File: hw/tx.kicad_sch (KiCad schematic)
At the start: 53 parts, among them Q301 IRLML2060, Q302 IRLML2060, Q303 IRLML2060, Q304 IRLML2060, T301 BN-43-202_DualPri_CTSec, U301 LCMXO2-256HC-4SG32C, U302 UCC27523DGN, U303 UCC27523DGN, U304 SI5351A-B-GT, Y301 20MHz

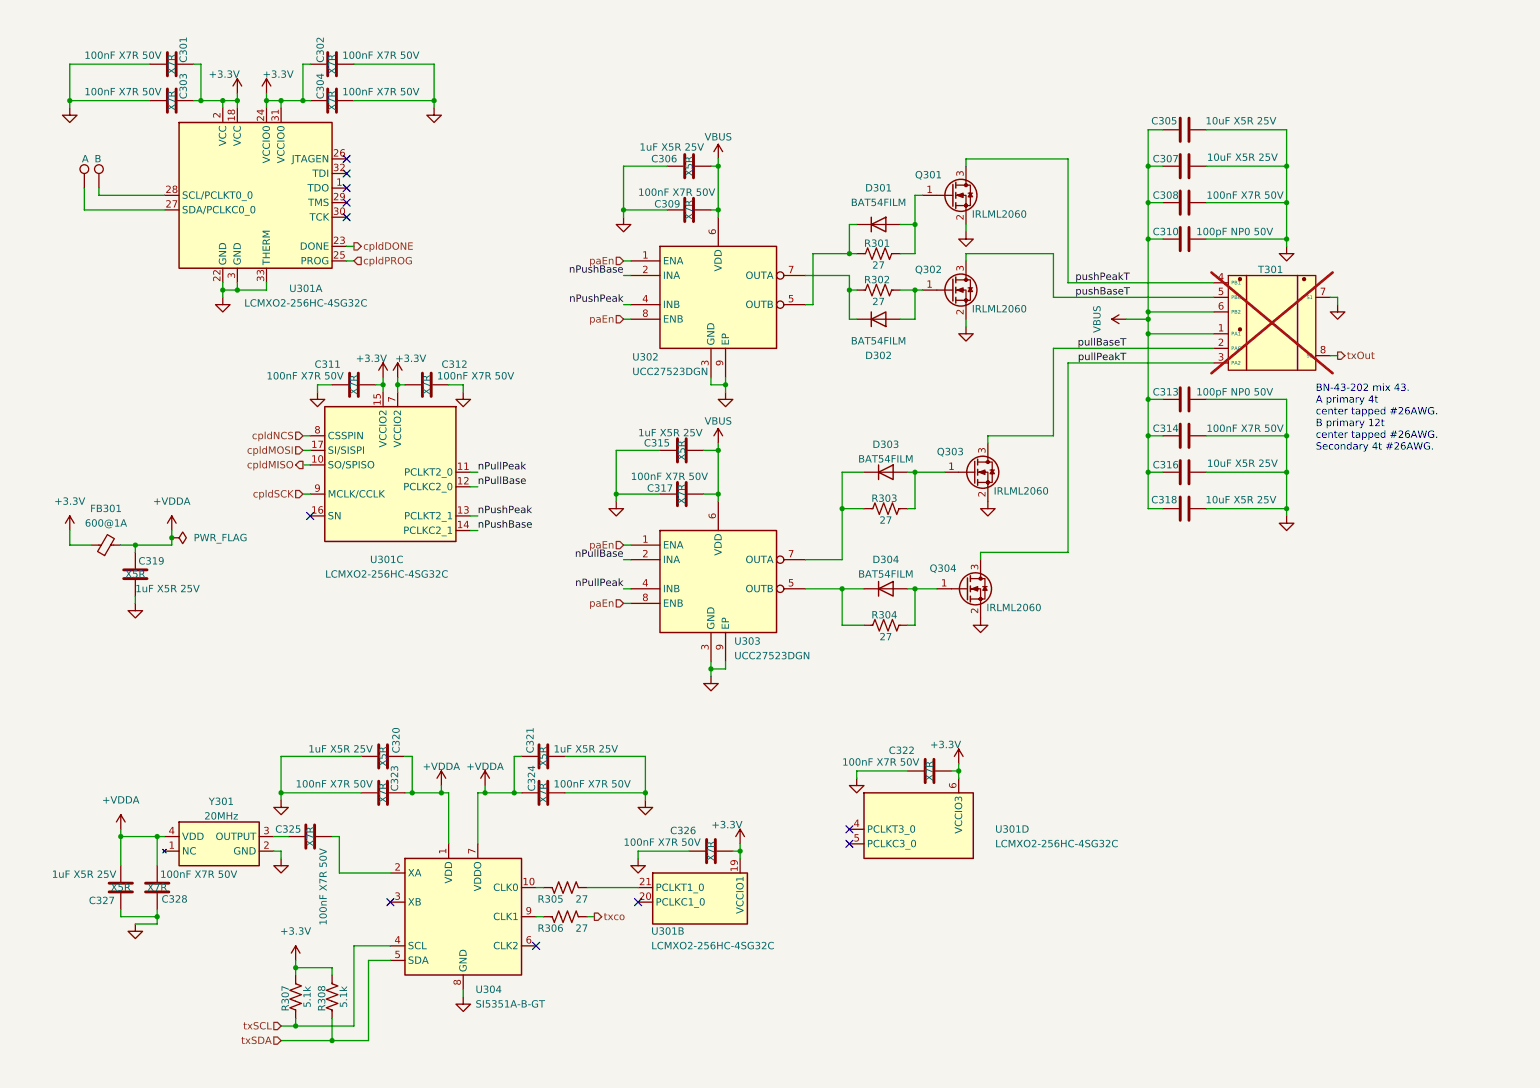
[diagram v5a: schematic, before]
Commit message: Prep to go back to FPGA. Board is routed except for power layer zones. No time to run DRC yet.
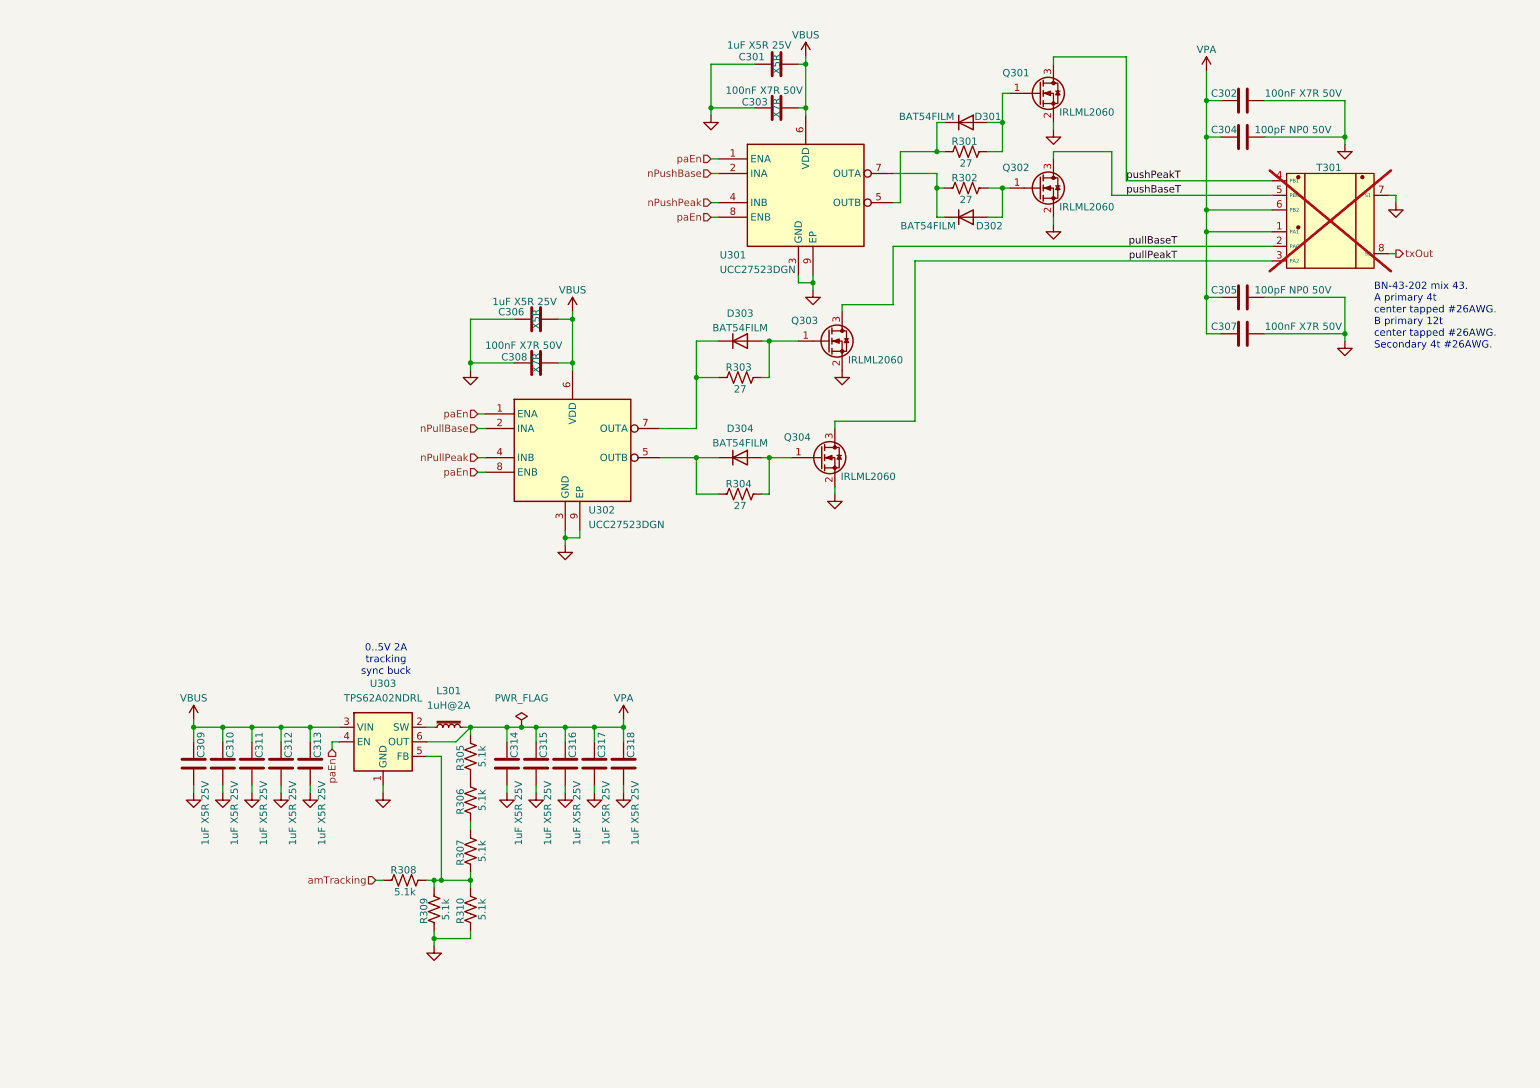
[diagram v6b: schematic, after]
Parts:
- removed C301, C302, C303, C304, C322, C323, C324, C325, C326, C328: 100nF X7R 50V, Capacitor_SMD:C_0402_1005Metric, symbol Device:C
- removed C305, C307: 10uF X5R 25V, Capacitor_SMD:C_0603_1608Metric, symbol Device:C
- removed C319, C320, C321, C327: 1uF X5R 25V, Capacitor_SMD:C_0402_1005Metric, symbol Device:C
- removed FB301: 600@1A, Inductor_SMD:L_0603_1608Metric, symbol Device:FerriteBead_Small
- removed TP301: A, TestPoint:TestPoint_Pad_1.5x1.5mm, symbol Connector:TestPoint
- removed TP302: B, TestPoint:TestPoint_Pad_1.5x1.5mm, symbol Connector:TestPoint
- removed U301: LCMXO2-256HC-4SG32C, Package_DFN_QFN:QFN-32-1EP_5x5mm_P0.5mm_EP3.1x3.1mm_ThermalVias, symbol Library:LCMXO2-SG32
- removed U304: SI5351A-B-GT, Package_SO:MSOP-10_3x3mm_P0.5mm, symbol Oscillator:Si5351A-B-GT
- removed Y301: 20MHz, Library:ECSTXO201633400TR, symbol Library:ECS-TX-5032-200
- added C309, C310, C313, C314, C315, C317: 1uF X5R 25V, Capacitor_SMD:C_0402_1005Metric, symbol Device:C
- added L301: 1uH@2A, Library:PFL4514-inductor, symbol Device:L_Iron_Small
- added R309, R310: 5.1k, Resistor_SMD:R_0402_1005Metric, symbol Device:R_US
- added U303: TPS62A02NDRL, Package_TO_SOT_SMD:SOT-563, symbol Regulator_Switching:TPS62A02NDRL
- C311, C312: value 100nF X7R 50V -> 1uF X5R 25V; LCSC (none) -> C7393852; MPN KAM05FR71H104KH -> 04023D105MAT2A; Mouser_PN (none) -> 581-04023D105MAT2A; cap-type X7R -> X5R; working-voltage 50V -> 25V
- C316, C318: value 10uF X5R 25V -> 1uF X5R 25V; footprint Capacitor_SMD:C_0603_1608Metric -> Capacitor_SMD:C_0402_1005Metric; LCSC C479655 -> C7393852; MPN CM105X5R106M25AT -> 04023D105MAT2A; Mouser_PN 346-CM105X5R106M25AT -> 581-04023D105MAT2A
- R301, R302, R303, R304: LCSC (none) -> C2906874; MFG (none) -> Vishay; MPN (none) -> MCS04020C5101FE000; Mouser_PN (none) -> 594-MCS04020C5101FE0
- R305, R306: value 27 -> 5.1k; LCSC C2906874 -> (none); MFG Vishay -> (none); MPN MCS04020C5101FE000 -> (none); Mouser_PN 594-MCS04020C5101FE0 -> (none)
- R307, R308: LCSC C2906874 -> (none); MFG Vishay -> (none); MPN MCS04020C5101FE000 -> (none); Mouser_PN 594-MCS04020C5101FE0 -> (none)
- renumbered C306 to C301, C308 to C302, C309 to C303, C310 to C304, C313 to C305, C315 to C306, C314 to C307, C317 to C308, U302 to U301, U303 to U302
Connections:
- net GND: now also C311.2, C312.2, C309.2, C310.2, C313.2, C314.2, C315.2, C317.2, R309.1, R310.1, U303.1 (GND); no longer C311.1, C312.1
- net VBUS: now also C311.1, C312.1, C309.1, C310.1, C313.1, U303.3 (VIN); no longer C302.1, C304.1, C305.1, C307.1, C316.1, C318.1, T301.1 (PA1), T301.6 (PB2)
- net paEn: now also U303.4 (EN)
- net at R305.1: now also R306.2
- net VPA: now reaches R305.2
- net VPA: now also C302.1, C304.1, C305.1, C307.1, C316.1, C318.1, T301.1 (PA1), T301.6 (PB2), C314.1, C315.1, C317.1, L301.2, U303.6 (OUT)
- removed net +3.3V: C311.2, C312.2, R307.2, R308.2
- net txSCL: no longer names the net of R307.1
- net txSCL: now also R308.2, R309.2, R310.2, U303.5 (FB)
- net txSDA renamed amTracking
- net txco: no longer names the net of R306.1
- net txco: now also R307.2
- new net: L301.1, U303.2 (SW)
- no-connect marks 11 -> 0
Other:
- note added: "0..5V 2A tracking sync buck"
- moved on the sheet: C301, C302, C303, C304, C305, C306, C307, C308, D301, D302, D303, D304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
